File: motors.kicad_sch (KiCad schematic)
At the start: 0 parts

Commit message: Test file
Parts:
- added U?: DRV8231DSGR, Package_SON:WSON-8-1EP_2x2mm_P0.5mm_EP0.9x1.6mm, symbol DRV8321:DRV8231DSGR
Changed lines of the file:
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@@
 (kicad_sch (version 20211123) (generator eeschema)
   (paper "A4")
+  (symbol (lib_id "DRV8321:DRV8231DSGR") (at 36.83 40.64 0) (unit 1)
+    (in_bom yes) (on_board yes) (fields_autoplaced)
+    (property "Reference" "U?" (id 0) (at 57.15 29.21 0)
+      (effects (font (size 1.524 1.524)))
+    )
+    (property "Value" "DRV8231DSGR" (id 1) (at 57.15 33.02 0)
+      (effects (font (size 1.524 1.524)))
+    )
+    (property "Footprint" "Package_SON:WSON-8-1EP_2x2mm_P0.5mm_EP0.9x1.6mm" (id 2) (at 57.15 34.544 0)
+      (effects (font (size 1.524 1.524)) hide)
+    )
+    (property "Datasheet" "" (id 3) (at 36.83 40.64 0)
+      (effects (font (size 1.524 1.524)))
+    )
+    (pin "1")
+    (pin "2")
+    (pin "3")
+    (pin "4")
+    (pin "5")
+    (pin "6")
+    (pin "7")
+    (pin "8")
+    (pin "9")
+  )
 )

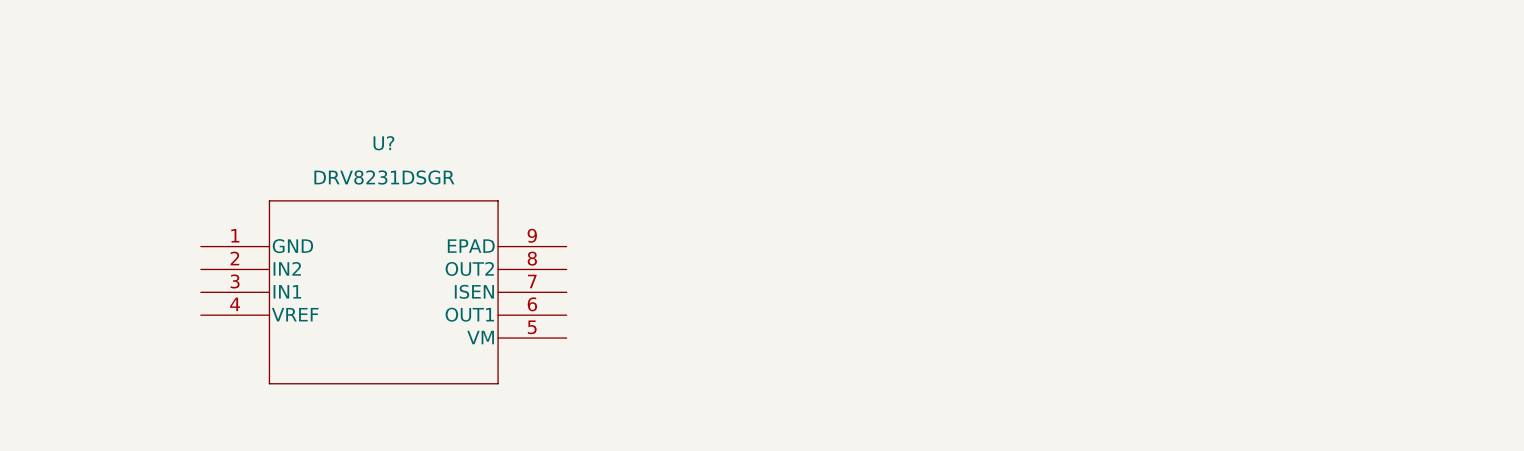
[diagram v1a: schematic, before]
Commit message: add JST connectors - add motors schematic
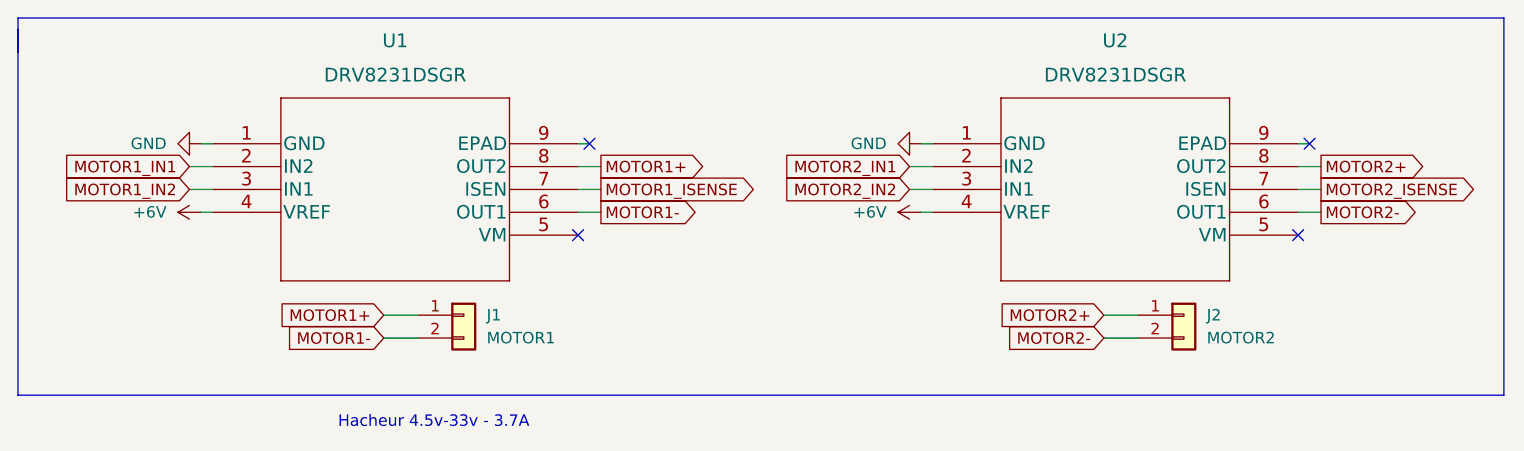
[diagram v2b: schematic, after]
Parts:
- added J1: MOTOR1, symbol Connector_Generic:Conn_01x02
- added J2: MOTOR2, symbol Connector_Generic:Conn_01x02
- added U2: DRV8231DSGR, Package_SON:WSON-8-1EP_2x2mm_P0.5mm_EP0.9x1.6mm, symbol DRV8321:DRV8231DSGR
- gave numbers to parts that had none: 1
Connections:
- net GND: now reaches U1.1 (GND)
- net GND: now also U2.1 (GND)
- net MOTOR1_IN1: now reaches U1.2 (IN2)
- net MOTOR1_IN2: now reaches U1.3 (IN1)
- net +6V: now reaches U1.4 (VREF)
- net +6V: now also U2.4 (VREF)
- net MOTOR1-: now reaches U1.6 (OUT1)
- net MOTOR1-: now also J1.2 (Pin_2)
- net MOTOR1_ISENSE: now reaches U1.7 (ISEN)
- net MOTOR1+: now reaches U1.8 (OUT2)
- net MOTOR1+: now also J1.1 (Pin_1)
- new net MOTOR2+: J2.1 (Pin_1), U2.8 (OUT2)
- new net MOTOR2-: J2.2 (Pin_2), U2.6 (OUT1)
- new net MOTOR2_IN1: U2.2 (IN2)
- new net MOTOR2_IN2: U2.3 (IN1)
- new net MOTOR2_ISENSE: U2.7 (ISEN)
- no-connect marks 0 -> 4
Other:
- note added: "Hacheur 4.5v-33v - 3.7A"
- moved on the sheet: U1

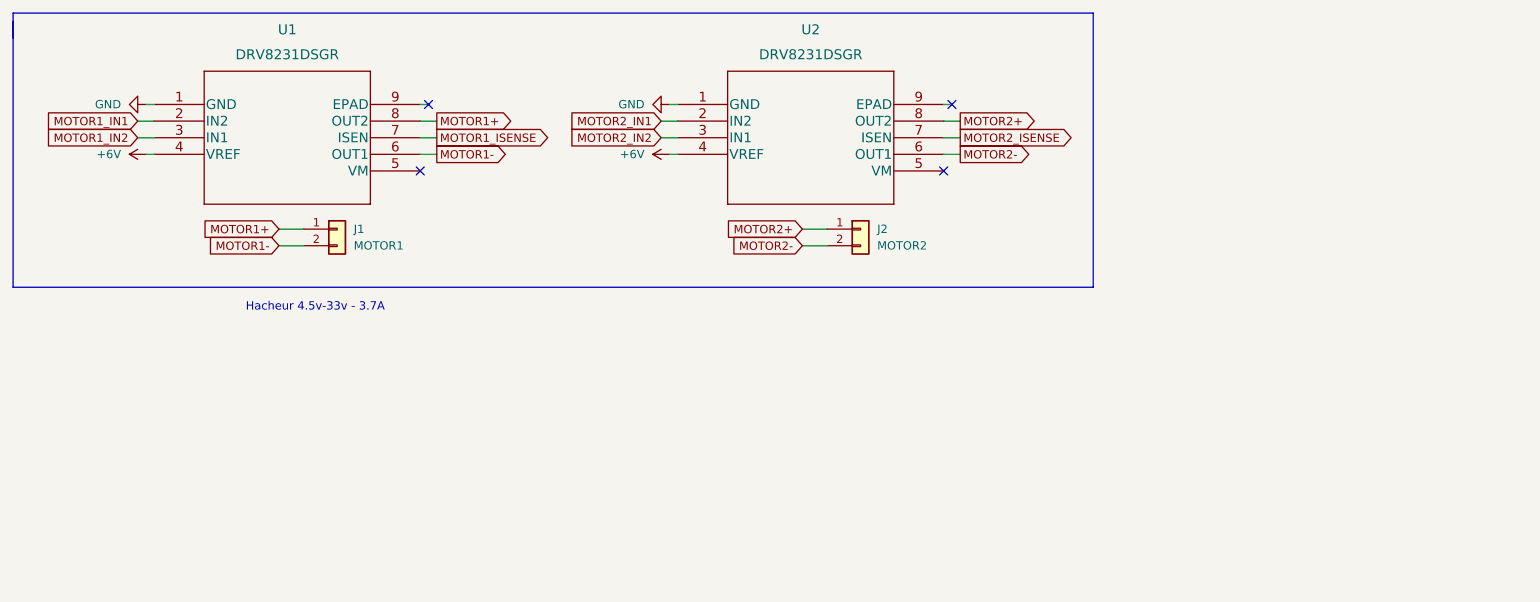
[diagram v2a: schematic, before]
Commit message: configure Isense pins
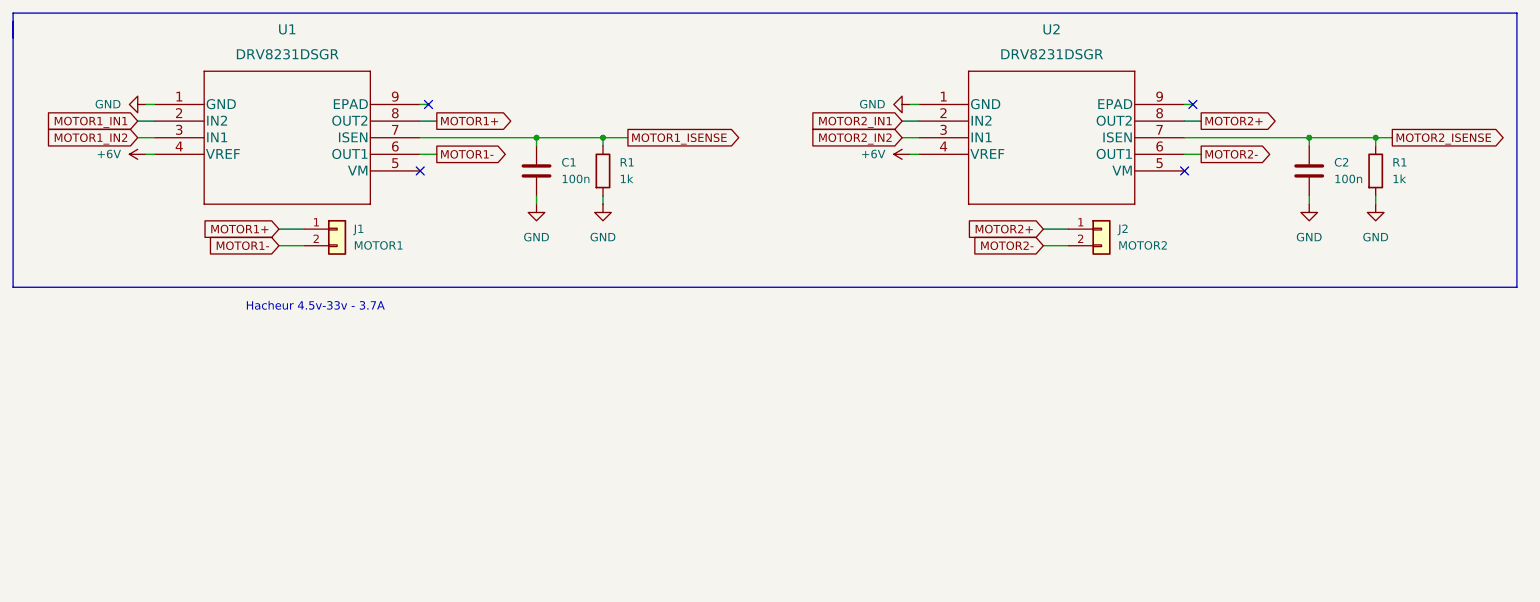
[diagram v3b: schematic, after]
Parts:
- added C1, C2: 100n, symbol Device:C
- added R1 (x2): 1k, symbol Device:R
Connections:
- net GND: now also C1.2, C2.2, R1.2, R1.2
- net MOTOR1_ISENSE: now also C1.1, R1.1
- net MOTOR2_ISENSE: now also C2.1, R1.1
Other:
- moved on the sheet: J2, U2

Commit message: add encoders and correct drivers
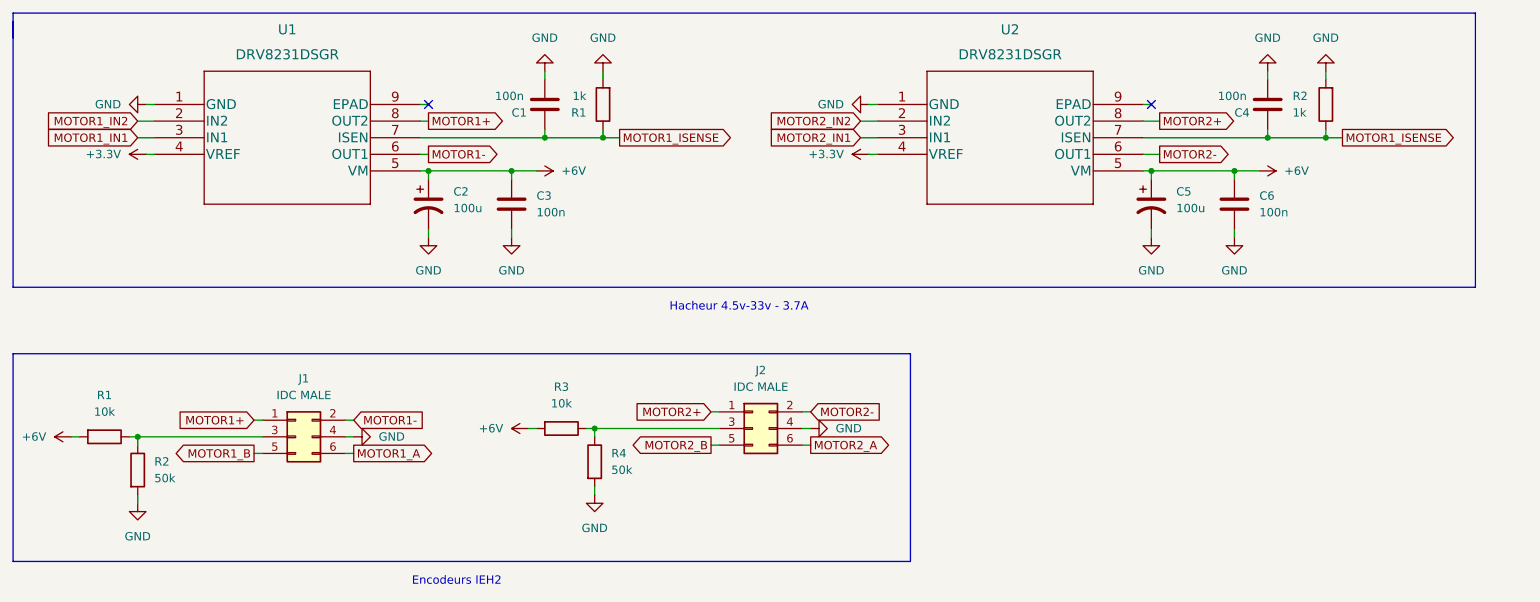
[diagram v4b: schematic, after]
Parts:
- removed C2: 100n, symbol Device:C
- removed J1: MOTOR1, symbol Connector_Generic:Conn_01x02
- removed J2: MOTOR2, symbol Connector_Generic:Conn_01x02
- added C2, C5: 100u, symbol Device:C_Polarized_US
- added C3, C4, C6: 100n, symbol Device:C
- added J1, J2: IDC MALE, symbol Connector_Generic:Conn_02x03_Odd_Even
- added R2: 1k, symbol Device:R
- added R2, R4: 50k, symbol Device:R
- added R3: 10k, symbol Device:R
- R1: value 1k -> 10k
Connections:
- net +6V: now also R1.2, U1.5 (VM), U2.5 (VM), C2.1, C3.1, C5.1, C6.1, R3.2; no longer U1.4 (VREF), U2.4 (VREF)
- net GND: now also C1.1, C2.2, C3.2, C4.1, C5.2, C6.2, J1.4 (Pin_4), J2.4 (Pin_4), R2.2, R2.2, R4.2; no longer C1.2, R1.2
- net MOTOR1+: now also J1.1 (Pin_1)
- net MOTOR1-: now also J1.2 (Pin_2)
- net MOTOR1_IN1: now also U1.3 (IN1); no longer U1.2 (IN2)
- net MOTOR1_IN2: now also U1.2 (IN2); no longer U1.3 (IN1)
- net MOTOR1_ISENSE: now also C1.2, U2.7 (ISEN), C4.2, R2.1; no longer C1.1
- net MOTOR2+: now also J2.1 (Pin_1)
- net MOTOR2-: now also J2.2 (Pin_2)
- net MOTOR2_IN1: now also U2.3 (IN1); no longer U2.2 (IN2)
- net MOTOR2_IN2: now also U2.2 (IN2); no longer U2.3 (IN1)
- net MOTOR2_ISENSE: no longer names the net of R1.1
- net MOTOR2_ISENSE: now also J1.3 (Pin_3), R2.1; no longer U2.7 (ISEN)
- new net: J2.3 (Pin_3), R3.1, R4.1
- new net +3.3V: U1.4 (VREF), U2.4 (VREF)
- new net MOTOR1_A: J1.6 (Pin_6)
- new net MOTOR1_B: J1.5 (Pin_5)
- new net MOTOR2_A: J2.6 (Pin_6)
- new net MOTOR2_B: J2.5 (Pin_5)
- no-connect marks 4 -> 2
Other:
- note added: "Encodeurs IEH2"
- moved on the sheet: R1, U2

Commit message: merge files for presentation
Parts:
- U4: renamed from U1; footprint Package_SON:WSON-8-1EP_2x2mm_P0.5mm_EP0.9x1.6mm -> DRV8231ADSGR:SON50P200X200X80-9N
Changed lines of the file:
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@@
   (symbol (lib_id "DRV8321:DRV8231DSGR") (at 38.1 29.21 0) (unit 1)
     (in_bom yes) (on_board yes) (fields_autoplaced)
-    (property "Reference" "U1" (id 0) (at 58.42 17.78 0)
+    (property "Reference" "U4" (id 0) (at 58.42 17.78 0)
       (effects (font (size 1.524 1.524)))
     )
@@
       (effects (font (size 1.524 1.524)))
     )
-    (property "Footprint" "Package_SON:WSON-8-1EP_2x2mm_P0.5mm_EP0.9x1.6mm" (id 2) (at 58.42 23.114 0)
+    (property "Footprint" "DRV8231ADSGR:SON50P200X200X80-9N" (id 2) (at 58.42 23.114 0)
       (effects (font (size 1.524 1.524)) hide)
     )
